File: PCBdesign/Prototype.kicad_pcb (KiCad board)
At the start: 2 copper layers, 15 parts, among them J1 AudioJack2, J2 Adafruit Micro-Lipo, SW2 SW_Nidec_CAS-120A1, U1 ESP32-S3-WROOM-2, U2 ER_OLEDM0.91_1x-I2C, U3 AP2112K-3.3, U4 MAX98357A, U5 PCM5102A

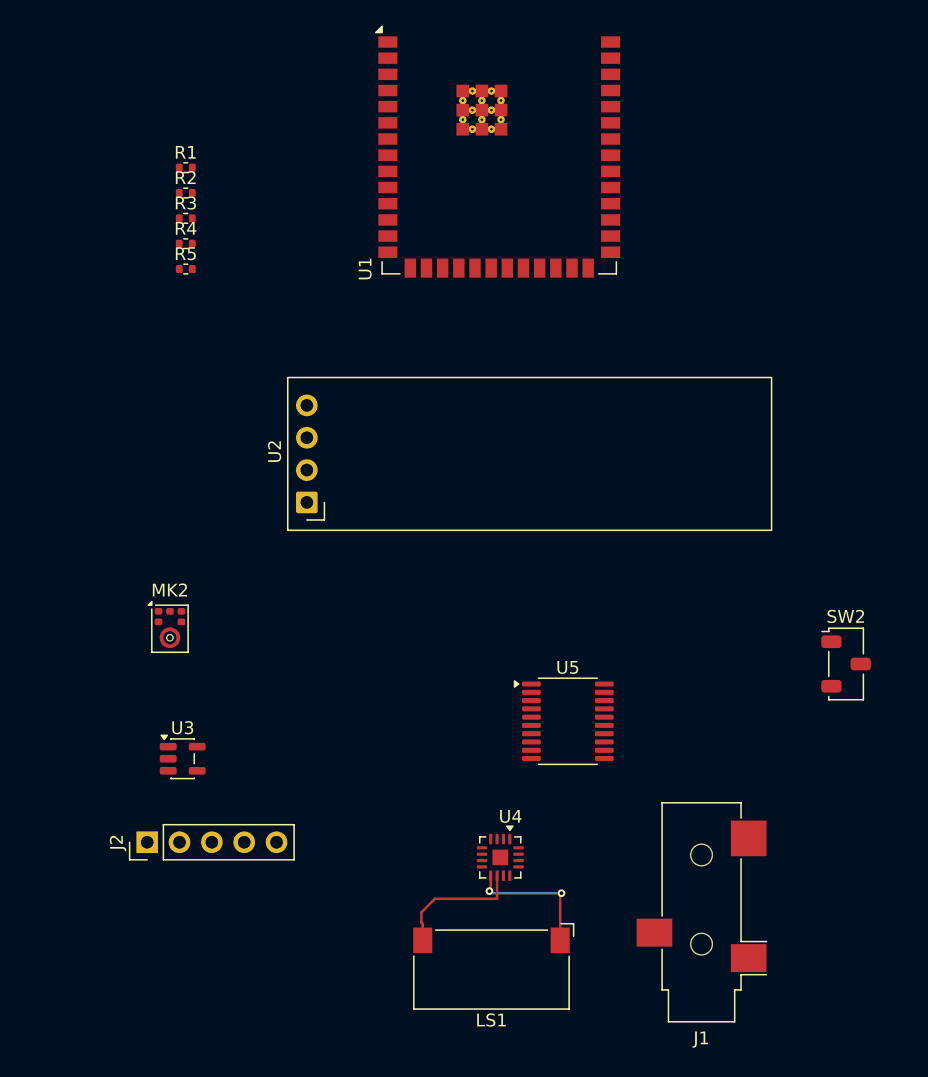
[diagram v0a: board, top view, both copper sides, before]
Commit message: Update PCB layout and schematic fixes
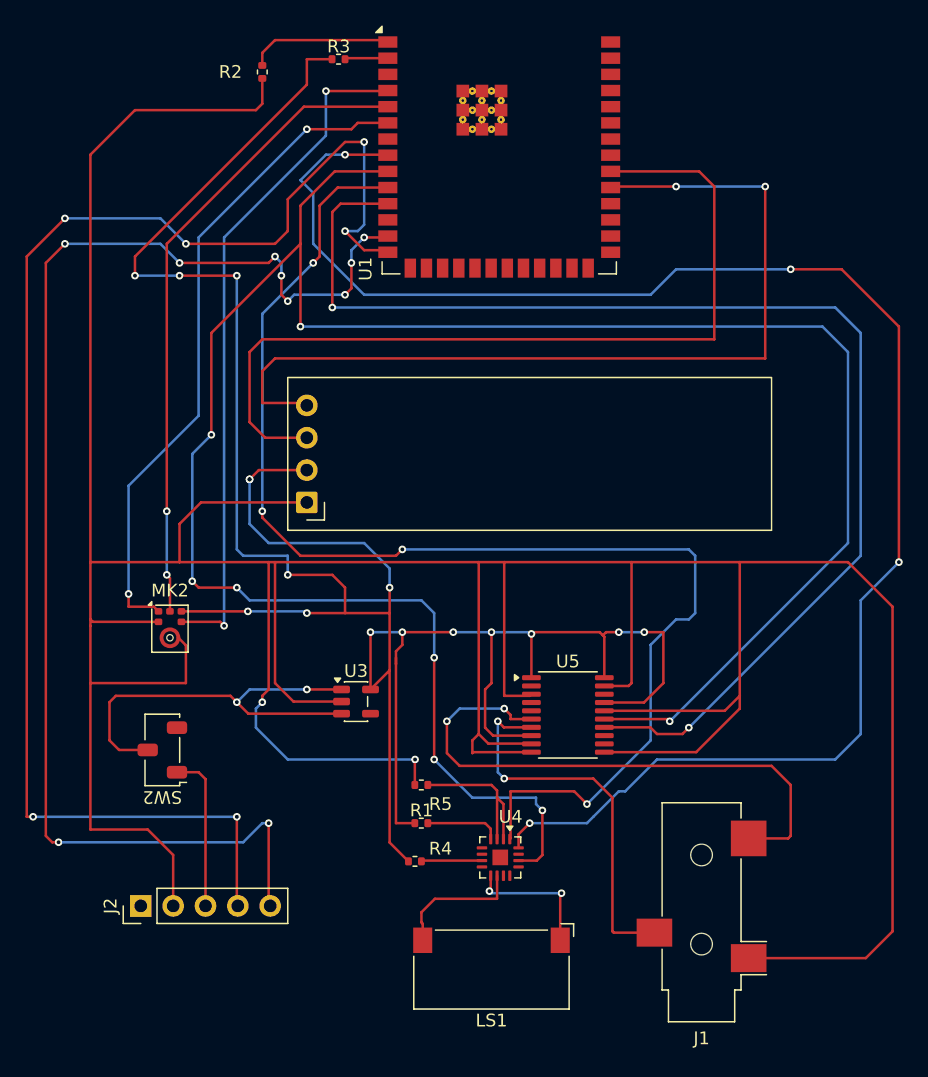
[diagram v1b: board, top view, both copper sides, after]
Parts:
- moved R1 54.7 mm to (125.5, 81.5)
- moved SW2 54.1 mm to (105.2, 75.8), turned to 180 degrees
- moved R4 51.7 mm to (125.0, 84.5), turned to 180 degrees
- moved R5 44.5 mm to (125.5, 78.5), turned to 180 degrees
- moved R3 17.3 mm to (119.0, 21.5), turned to 180 degrees
- moved U3 14.3 mm to (120.4, 72.0)
- moved R2 11.2 mm to (113.0, 22.5), turned to 90 degrees
- moved J2 5.02 mm to (103.5, 88.0)
- moved U5 0.50 mm to (137.0, 73.0)
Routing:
- net Net-(J2-GND): track 0.00 -> 324.0 mm
- net Net-(MK2-VDD): track 0.00 -> 190.2 mm, vias 0 -> 15
- net Net-(U1-IO16): track 0.00 -> 178.9 mm, vias 0 -> 8
- net Net-(U1-IO15): track 0.00 -> 127.9 mm, vias 0 -> 4
- net Net-(J2-D+): track 0.00 -> 113.1 mm, vias 0 -> 6
- net Net-(J2-D-): track 0.00 -> 105.0 mm, vias 0 -> 10
- net Net-(U1-IO17): track 0.00 -> 101.8 mm, vias 0 -> 4
- net Net-(U1-IO18): track 0.00 -> 98.1 mm, vias 0 -> 2
- net Net-(U1-IO38): track 0.00 -> 71.7 mm, vias 0 -> 2
- net Net-(U1-MTCK/IO39): track 0.00 -> 68.1 mm
- net Net-(MK2-BCLK): track 0.00 -> 53.7 mm, vias 0 -> 2
- net Net-(MK2-WS): track 0.00 -> 52.4 mm, vias 0 -> 2
- net Net-(MK2-DATA): track 0.00 -> 50.8 mm, vias 0 -> 2
- net Net-(U2-VCC): track 0.00 -> 46.5 mm, vias 0 -> 3
- net Net-(U5-OUTL): track 0.00 -> 45.5 mm, vias 0 -> 2
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
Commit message: Describe your updates here
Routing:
- net Net-(U2-VCC): track 46.5 -> 45.9 mm
